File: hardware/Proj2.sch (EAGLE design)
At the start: 20 parts, among them IC1 2985-A4988

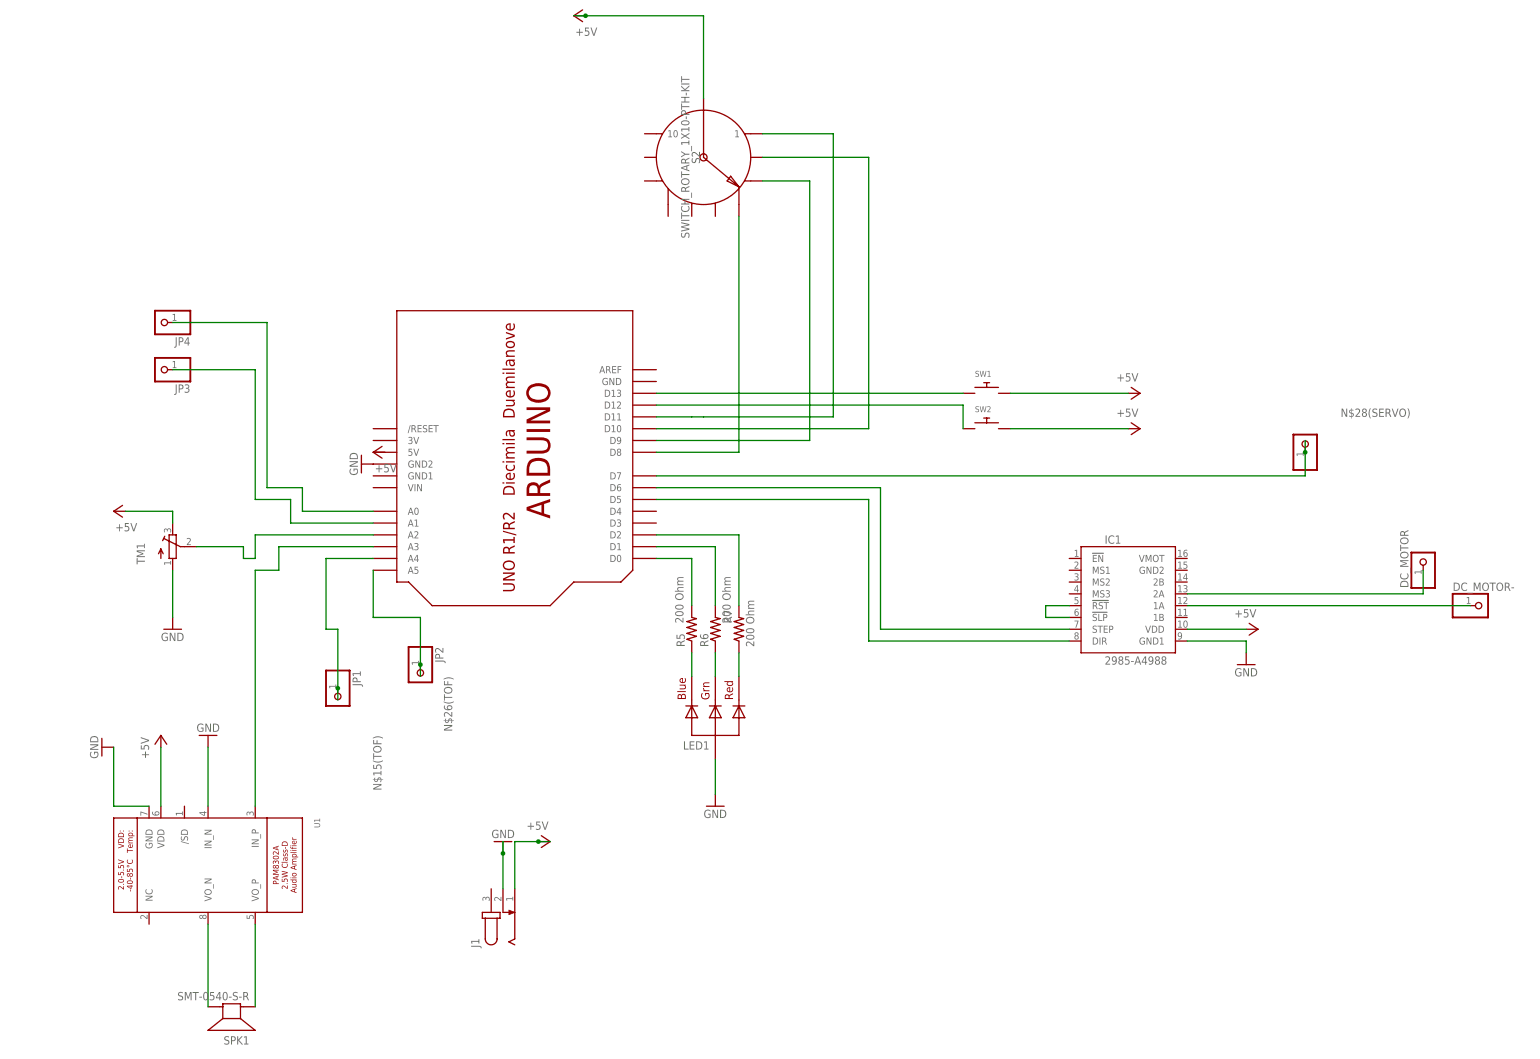
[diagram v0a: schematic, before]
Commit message: Revise schematic to use pin headers and other connectors, correct motor driver, and resistor ladder for rotary switch
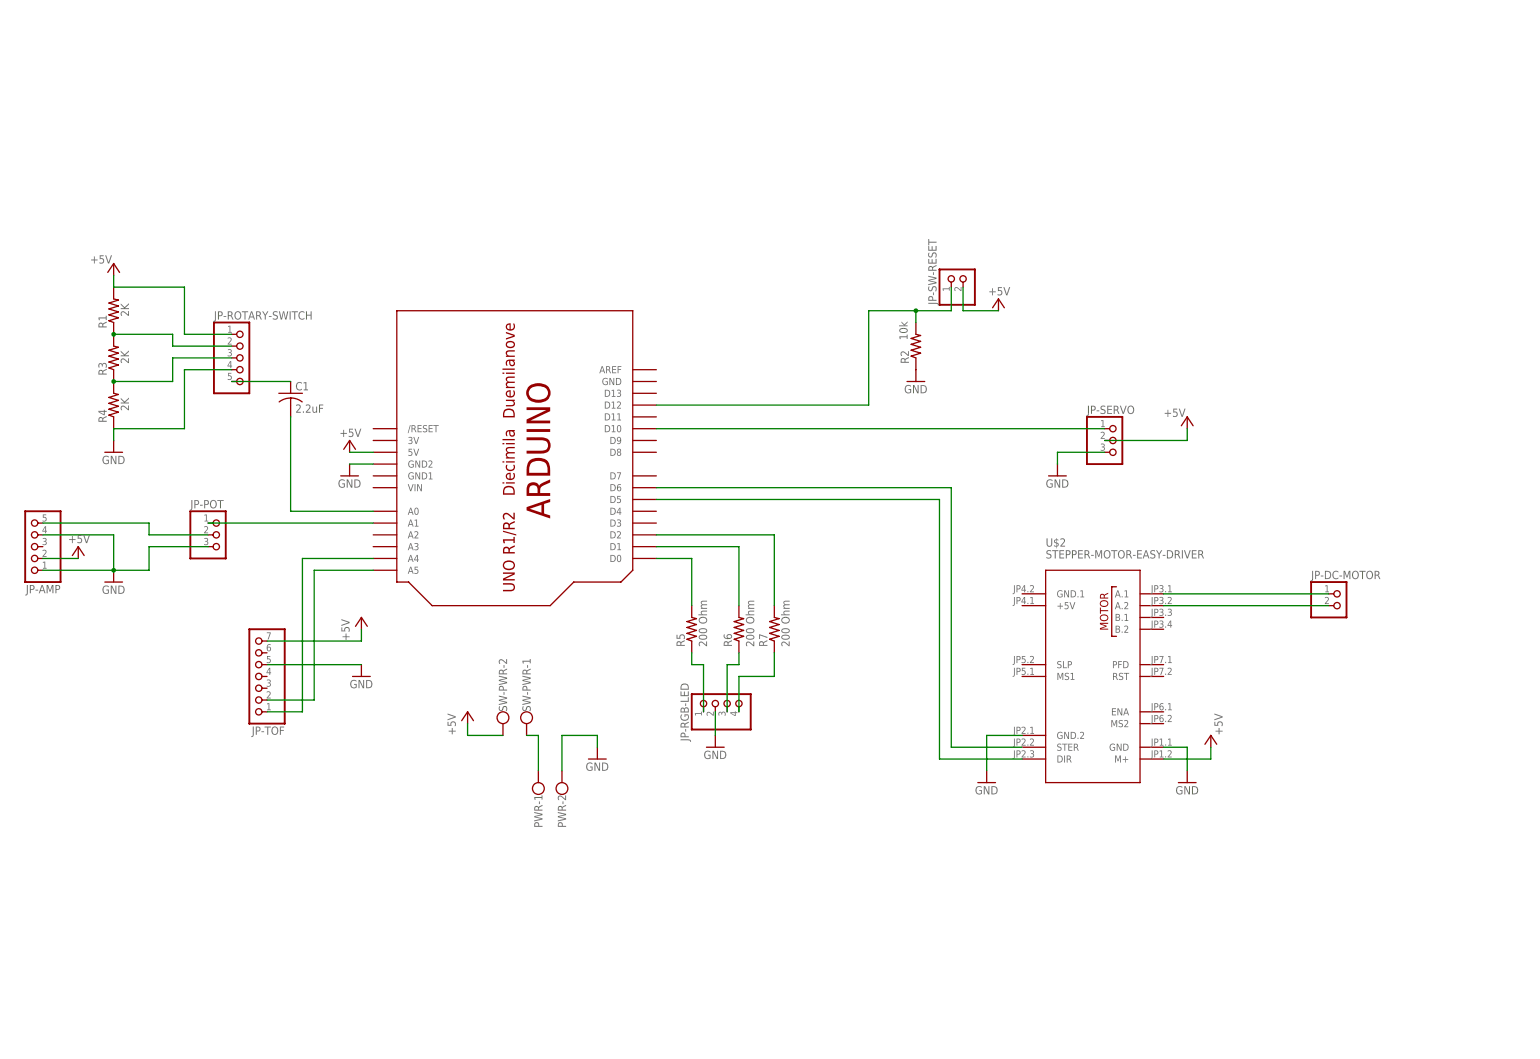
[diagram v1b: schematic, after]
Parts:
- removed DC_MOTOR, DC_MOTOR-, JP1, JP2, JP9: (no value), adafruit:PINHD-1X1
- removed IC1: 2985-A4988, pololu-stepper-driver:2985-A4988
- removed J1: (no value), con-jack:JACK-PLUG1
- removed JP3, JP4: (no value), pinhead:PINHD-1X1
- removed LED1: RGBLED_CA-PIRANHA, adafruit:RGBLED_CA-PIRANHA
- removed S2: SWITCH_ROTARY_1X10-PTH-KIT, SparkFun-Switches:SWITCH_ROTARY_1X10-PTH-KIT
- removed SPK1: SMT-0540-S-R, adafruit:SMT-0540-S-R
- removed SW1, SW2: (no value), adafruit:SWITCH_PUSHBUTTONEVQ-PE
- removed TM1: (no value), adafruit:TRIMPOT3386
- removed U1: (no value), Adafruit PAM8302:MICROBUILDER_AUDIOAMP_PAM8302A
- added C1: 2.2uF, rcl:C-US050-024X044
- added JP-AMP, JP-ROTARY-SWITCH: (no value), pinhead:PINHD-1X5
- added JP-DC-MOTOR, JP-SW-RESET: (no value), pinhead:PINHD-1X2
- added JP-POT, JP-SERVO: (no value), pinhead:PINHD-1X3
- added JP-RGB-LED: (no value), pinhead:PINHD-1X4
- added JP-TOF: (no value), pinhead:PINHD-1X7
- added PWR, SW-PWR: (no value), con-wago-500:W237-102
- added R1, R3, R4: 2K, adafruit:R-US_0207/7
- added R2: 10k, adafruit:R-US_0207/7
- added U$2: STEPPER-MOTOR-EASY-DRIVER, diy-modules:STEPPER-MOTOR-EASY-DRIVER
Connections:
- removed net N$15(TOF): JP1.1, U$1.A4
- removed net N$18: LED1.BLUE, R5.1
- removed net N$26(TOF): JP2.1, U$1.A5
- removed net N$28(SERVO): JP9.1, U$1.D7
- removed net N$5: IC1.!RST, IC1.!SLP
- new net N$14: JP-SW-RESET.1, R2.2, U$1.D12
- new net N$15: JP-RGB-LED.4, R7.1
- net +5V: now also JP-AMP.2, JP-SERVO.2, JP-SW-RESET.2, JP-TOF.7, SW-PWR-2.KL, U$1.5V, U$2.M+; no longer IC1.VDD, J1.1, S2.COMMON, SW1.P$2, SW2.P$2, TM1.E, U1.VDD
- net GND: now also JP-AMP.1, JP-AMP.4, JP-POT.3, JP-RGB-LED.2, JP-SERVO.3, JP-TOF.5, PWR-2.KL, R2.1, U$2.GND, U$2.GND.2; no longer IC1.GND1, J1.2, LED1.VCC, TM1.A, U1.GND, U1.IN_N
- net N$1: now also JP-TOF.1, U$1.A4; no longer SPK1.+, U1.VO_P
- net N$12: now also U$2.DIR; no longer IC1.DIR
- net N$13: now also JP-POT.1, U$1.A1; no longer TM1.S, U$1.A2
- net N$16: now also C1.2, U$1.A0; no longer JP3.1, U$1.A1
- net N$17: now also JP-AMP.5, JP-POT.2; no longer JP4.1, U$1.A0
- net N$19: now also JP-ROTARY-SWITCH.2, R1.1, R3.2; no longer LED1.GREEN, R6.1
- net N$2: now also JP-TOF.2, U$1.A5; no longer SPK1.-, U1.VO_N
- net N$20: now also JP-ROTARY-SWITCH.3, R3.1, R4.2; no longer LED1.RED, R7.1
- net N$21: now also U$2.STER; no longer IC1.STEP
- net N$22: now also JP-ROTARY-SWITCH.1, R1.2; no longer S2.3, U$1.D9
- net N$23: now also JP-ROTARY-SWITCH.4, R4.1; no longer S2.4, U$1.D8
- net N$24: now also JP-DC-MOTOR.2, U$2.A.2; no longer DC_MOTOR-.1, IC1.1A
- net N$25: now also JP-DC-MOTOR.1, U$2.A.1; no longer DC_MOTOR.1, IC1.2A
- net N$3: now also PWR-1.KL, SW-PWR-1.KL; no longer SW1.P$1, U$1.D13
- net N$4: now also JP-RGB-LED.1, R5.1; no longer SW2.P$1, U$1.D12
- net N$6: now also C1.1, JP-ROTARY-SWITCH.5; no longer U$1.A3, U1.IN_P
- net N$8: now also JP-SERVO.1; no longer S2.2
- net N$9: now also JP-RGB-LED.3, R6.1; no longer S2.1, U$1.D11
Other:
- moved on the sheet: R6, R7

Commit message: Design PCB rev1
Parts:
- R5, R6, R7: value 200 Ohm -> 200
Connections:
- removed net N$22: JP-ROTARY-SWITCH.1, R1.2
- removed net N$23: JP-ROTARY-SWITCH.4, R4.1
- net +5V: now also JP-ROTARY-SWITCH.1, R1.2
- net GND: now also JP-ROTARY-SWITCH.4, R4.1
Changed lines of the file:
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@@
 <part name="GND2" library="supply1" library_urn="urn:adsk.eagle:library:371" deviceset="GND" device=""/>
 <part name="P+2" library="supply1" library_urn="urn:adsk.eagle:library:371" deviceset="+5V" device=""/>
-<part name="R5" library="adafruit" library_urn="urn:adsk.eagle:library:420" deviceset="R-US_" device="0207/7" package3d_urn="urn:adsk.eagle:package:6240602/1" value="200 Ohm"/>
-<part name="R6" library="adafruit" library_urn="urn:adsk.eagle:library:420" deviceset="R-US_" device="0207/7" package3d_urn="urn:adsk.eagle:package:6240602/1" value="200 Ohm"/>
-<part name="R7" library="adafruit" library_urn="urn:adsk.eagle:library:420" deviceset="R-US_" device="0207/7" package3d_urn="urn:adsk.eagle:package:6240602/1" value="200 Ohm"/>
+<part name="R5" library="adafruit" library_urn="urn:adsk.eagle:library:420" deviceset="R-US_" device="0207/7" package3d_urn="urn:adsk.eagle:package:6240602/1" value="200"/>
+<part name="R6" library="adafruit" library_urn="urn:adsk.eagle:library:420" deviceset="R-US_" device="0207/7" package3d_urn="urn:adsk.eagle:package:6240602/1" value="200"/>
+<part name="R7" library="adafruit" library_urn="urn:adsk.eagle:library:420" deviceset="R-US_" device="0207/7" package3d_urn="urn:adsk.eagle:package:6240602/1" value="200"/>
 <part name="P+6" library="supply1" library_urn="urn:adsk.eagle:library:371" deviceset="+5V" device=""/>
 <part name="GND1" library="supply1" library_urn="urn:adsk.eagle:library:371" deviceset="GND" device=""/>
@@
 <wire x1="-810.26" y1="449.58" x2="-810.26" y2="452.12" width="0.1524" layer="91"/>
 </segment>
+<segment>
+<pinref part="JP-ROTARY-SWITCH" gate="A" pin="1"/>
+<wire x1="-1021.08" y1="541.02" x2="-1031.24" y2="541.02" width="0.1524" layer="91"/>
+<wire x1="-1031.24" y1="541.02" x2="-1031.24" y2="551.18" width="0.1524" layer="91"/>
+<pinref part="R1" gate="G$1" pin="2"/>
+<wire x1="-1031.24" y1="551.18" x2="-1046.48" y2="551.18" width="0.1524" layer="91"/>
+<pinref part="P+1" gate="1" pin="+5V"/>
+<wire x1="-1046.48" y1="553.72" x2="-1046.48" y2="551.18" width="0.1524" layer="91"/>
+<junction x="-1046.48" y="551.18"/>
+</segment>
 </net>
 <net name="N$8" class="0">
@@
 <wire x1="-815.34" y1="452.12" x2="-815.34" y2="447.04" width="0.1524" layer="91"/>
 </segment>
+<segment>
+<pinref part="JP-ROTARY-SWITCH" gate="A" pin="4"/>
+<wire x1="-1021.08" y1="533.4" x2="-1031.24" y2="533.4" width="0.1524" layer="91"/>
+<wire x1="-1031.24" y1="533.4" x2="-1031.24" y2="520.7" width="0.1524" layer="91"/>
+<pinref part="R4" gate="G$1" pin="1"/>
+<wire x1="-1031.24" y1="520.7" x2="-1046.48" y2="520.7" width="0.1524" layer="91"/>
+<pinref part="GND10" gate="1" pin="GND"/>
+<wire x1="-1046.48" y1="520.7" x2="-1046.48" y2="518.16" width="0.1524" layer="91"/>
+<junction x="-1046.48" y="520.7"/>
+</segment>
 </net>
 <net name="N$7" class="0">
@@
 </segment>
 </net>
-<net name="N$22" class="0">
-<segment>
-<pinref part="JP-ROTARY-SWITCH" gate="A" pin="1"/>
-<wire x1="-1021.08" y1="541.02" x2="-1031.24" y2="541.02" width="0.1524" layer="91"/>
-<wire x1="-1031.24" y1="541.02" x2="-1031.24" y2="551.18" width="0.1524" layer="91"/>
-<pinref part="R1" gate="G$1" pin="2"/>
-<wire x1="-1031.24" y1="551.18" x2="-1046.48" y2="551.18" width="0.1524" layer="91"/>
-<pinref part="P+1" gate="1" pin="+5V"/>
-<wire x1="-1046.48" y1="553.72" x2="-1046.48" y2="551.18" width="0.1524" layer="91"/>
-</segment>
-</net>
-<net name="N$23" class="0">
-<segment>
-<pinref part="JP-ROTARY-SWITCH" gate="A" pin="4"/>
-<wire x1="-1021.08" y1="533.4" x2="-1031.24" y2="533.4" width="0.1524" layer="91"/>
-<wire x1="-1031.24" y1="533.4" x2="-1031.24" y2="520.7" width="0.1524" layer="91"/>
-<pinref part="R4" gate="G$1" pin="1"/>
-<wire x1="-1031.24" y1="520.7" x2="-1046.48" y2="520.7" width="0.1524" layer="91"/>
-<pinref part="GND10" gate="1" pin="GND"/>
-<wire x1="-1046.48" y1="520.7" x2="-1046.48" y2="518.16" width="0.1524" layer="91"/>
-</segment>
-</net>
 <net name="N$16" class="0">
 <segment>
@@
 </sheet>
 </sheets>
+<errors>
+</errors>
 </schematic>
 </drawing>

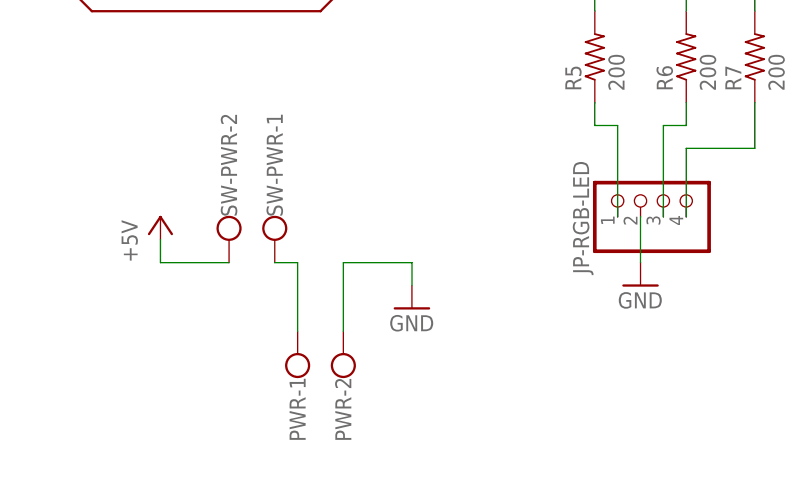
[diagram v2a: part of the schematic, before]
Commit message: Revisions from meeting, generate CAM files
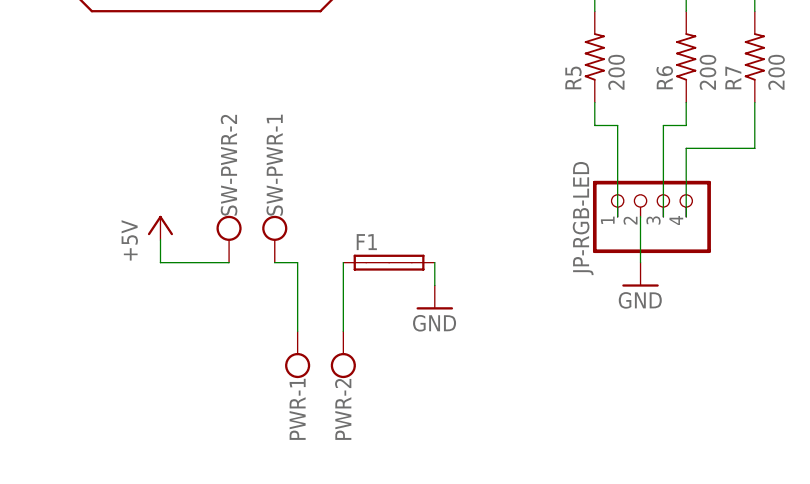
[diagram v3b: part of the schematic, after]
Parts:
- added F1: (no value), fuse:SHK20L
- U$1: value ARDUINO-BPLACE -> ARDUINO-NOHOLE; device adafruit:ARDUINO-BPLACE -> adafruit:ARDUINO-NOHOLE
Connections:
- new net N$5: F1.1A, PWR-2.KL
- net GND: now also F1.2A; no longer PWR-2.KL
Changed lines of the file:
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@@
 </classes>
 <parts>
-<part name="U$1" library="adafruit" library_urn="urn:adsk.eagle:library:420" deviceset="ARDUINO" device="-BPLACE" package3d_urn="urn:adsk.eagle:package:6240820/1"/>
+<part name="U$1" library="adafruit" deviceset="ARDUINO" device="-NOHOLE"/>
 <part name="GND2" library="supply1" library_urn="urn:adsk.eagle:library:371" deviceset="GND" device=""/>
 <part name="P+2" library="supply1" library_urn="urn:adsk.eagle:library:371" deviceset="+5V" device=""/>
@@
 <part name="U$2" library="diy-modules" deviceset="STEPPER-MOTOR-EASY-DRIVER" device=""/>
 <part name="GND5" library="supply1" library_urn="urn:adsk.eagle:library:371" deviceset="GND" device=""/>
+<part name="F1" library="fuse" library_urn="urn:adsk.eagle:library:233" deviceset="SHK20L" device="" package3d_urn="urn:adsk.eagle:package:14071/1"/>
 </parts>
 <sheets>
@@
 <attribute name="VALUE" x="-972.82" y="454.66" size="1.778" layer="96" rot="R90"/>
 </instance>
-<instance part="GND6" gate="1" x="-942.34" y="449.58" smashed="yes">
-<attribute name="VALUE" x="-944.88" y="447.04" size="1.778" layer="96"/>
+<instance part="GND6" gate="1" x="-939.8" y="449.58" smashed="yes">
+<attribute name="VALUE" x="-942.34" y="447.04" size="1.778" layer="96"/>
 </instance>
 <instance part="P+8" gate="1" x="-995.68" y="518.16" smashed="yes">
@@
 <instance part="GND5" gate="1" x="-858.52" y="444.5" smashed="yes">
 <attribute name="VALUE" x="-861.06" y="441.96" size="1.778" layer="96"/>
+</instance>
+<instance part="F1" gate="G$1" x="-944.88" y="454.66" smashed="yes">
+<attribute name="NAME" x="-948.69" y="456.057" size="1.778" layer="95"/>
+<attribute name="VALUE" x="-948.69" y="451.739" size="1.778" layer="96"/>
 </instance>
 </instances>
@@
 </segment>
 <segment>
-<wire x1="-949.96" y1="454.66" x2="-942.34" y2="454.66" width="0.1524" layer="91"/>
 <pinref part="GND6" gate="1" pin="GND"/>
-<wire x1="-942.34" y1="454.66" x2="-942.34" y2="452.12" width="0.1524" layer="91"/>
-<wire x1="-949.96" y1="454.66" x2="-949.96" y2="447.04" width="0.1524" layer="91"/>
-<pinref part="PWR" gate="-2" pin="KL"/>
+<wire x1="-939.8" y1="454.66" x2="-939.8" y2="452.12" width="0.1524" layer="91"/>
+<pinref part="F1" gate="G$1" pin="2A"/>
 </segment>
 <segment>
@@
 </segment>
 </net>
+<net name="N$5" class="0">
+<segment>
+<wire x1="-949.96" y1="454.66" x2="-949.96" y2="447.04" width="0.1524" layer="91"/>
+<pinref part="PWR" gate="-2" pin="KL"/>
+<pinref part="F1" gate="G$1" pin="1A"/>
+</segment>
+</net>

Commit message: Revise trace widths, power plane, fuse footprint after meeting with James
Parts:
- F1: device fuse:SHK20L -> fuse:SH32
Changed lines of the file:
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@@
 <part name="U$2" library="diy-modules" deviceset="STEPPER-MOTOR-EASY-DRIVER" device=""/>
 <part name="GND5" library="supply1" library_urn="urn:adsk.eagle:library:371" deviceset="GND" device=""/>
-<part name="F1" library="fuse" library_urn="urn:adsk.eagle:library:233" deviceset="SHK20L" device="" package3d_urn="urn:adsk.eagle:package:14071/1"/>
+<part name="F1" library="fuse" library_urn="urn:adsk.eagle:library:233" deviceset="SH32" device="" package3d_urn="urn:adsk.eagle:package:14068/1"/>
 </parts>
 <sheets>
